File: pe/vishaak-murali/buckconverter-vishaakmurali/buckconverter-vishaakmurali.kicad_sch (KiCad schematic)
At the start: 7 parts, among them J1 VIN_IN, J2 VOUT_5V, U1 AP63205WU

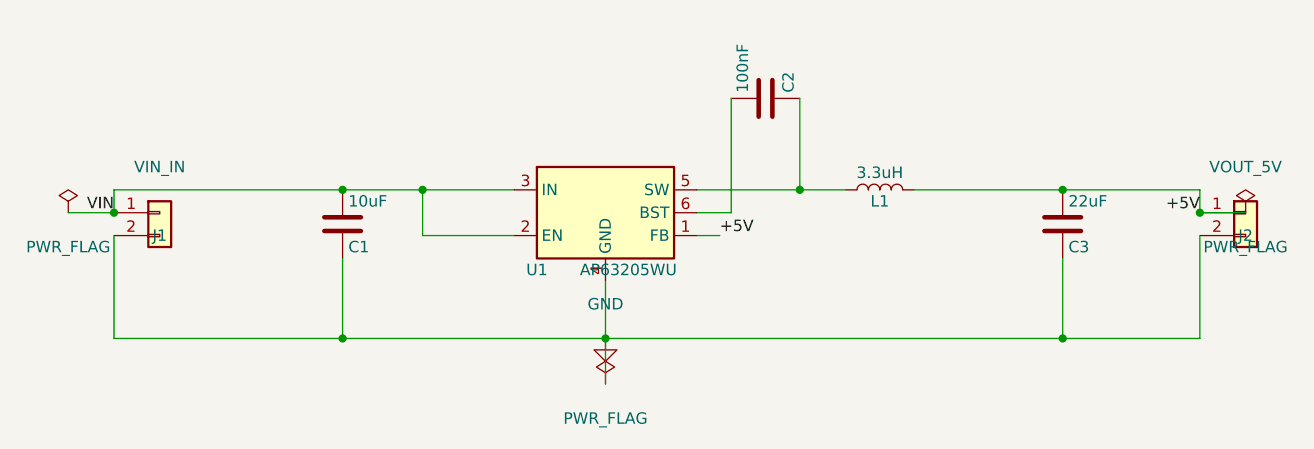
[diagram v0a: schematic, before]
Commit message: wip: swap buck converter to TI TPS54202
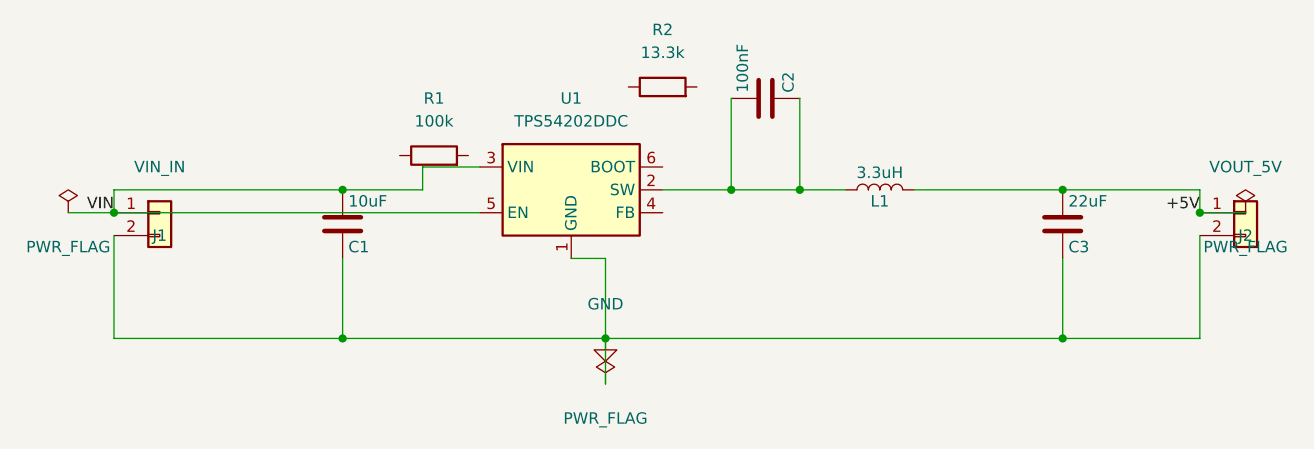
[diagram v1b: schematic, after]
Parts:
- removed U1: AP63205WU, Package_TO_SOT_SMD:TSOT-23-6, symbol Regulator_Switching:AP63205WU
- added R1: 100k, Resistor_SMD:R_0603_1608Metric, symbol Device:R
- added R2: 13.3k, Resistor_SMD:R_0603_1608Metric, symbol Device:R
- added U1: TPS54202DDC, Package_TO_SOT_SMD:SOT-23-6, symbol Regulator_Switching:TPS54202DDC
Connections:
- net GND: now also U1.1 (GND)
- net VIN: now also U1.3 (VIN), U1.5 (EN)
- net at C2.2, L1.1: now also C2.1, U1.2 (SW)
